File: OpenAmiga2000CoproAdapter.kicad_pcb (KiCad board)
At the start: 2 copper layers, 188.6 x 110.4 mm, 75 parts, among them CN1 A2000_COPRO_SLOT, P1 CONN_2, P10 CONN_1, P11 CONN_1, P12 CONN_1, P13 CONN_1, P14 CONN_1, P15 CONN_1, P2 CONN_2, P3 CONN_2, P4 CONN_2, P5 CONN_1, P6 CONN_1, P7 CONN_1, P8 CONN_1, P9 CONN_1, P99 OSHW_LOGO, U1 68000D, U10 Spare, U11 74HCT00, U12 74HCT27, U13 74HCT74, U14 74F86, U15 74F74, U16 74HCT04, U17 74HCT112, U18 74F157, U19 74F157, U2 AS6C4008-55PCN, U3 AS6C4008-55PCN, U4 AS6C4008-55PCN, U5 AS6C4008-55PCN, U6 74HCT00, U7 74HCT32, U8 74HCT32, U9 74LS05

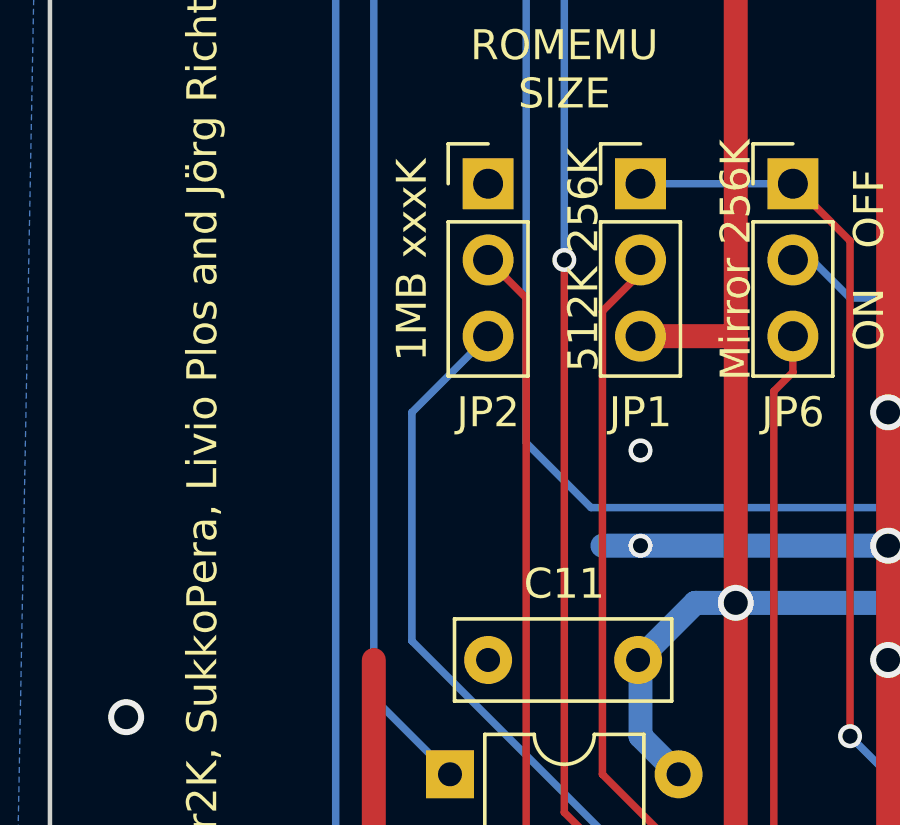
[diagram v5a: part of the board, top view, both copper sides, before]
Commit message: turn jumper around so it matches silk screen
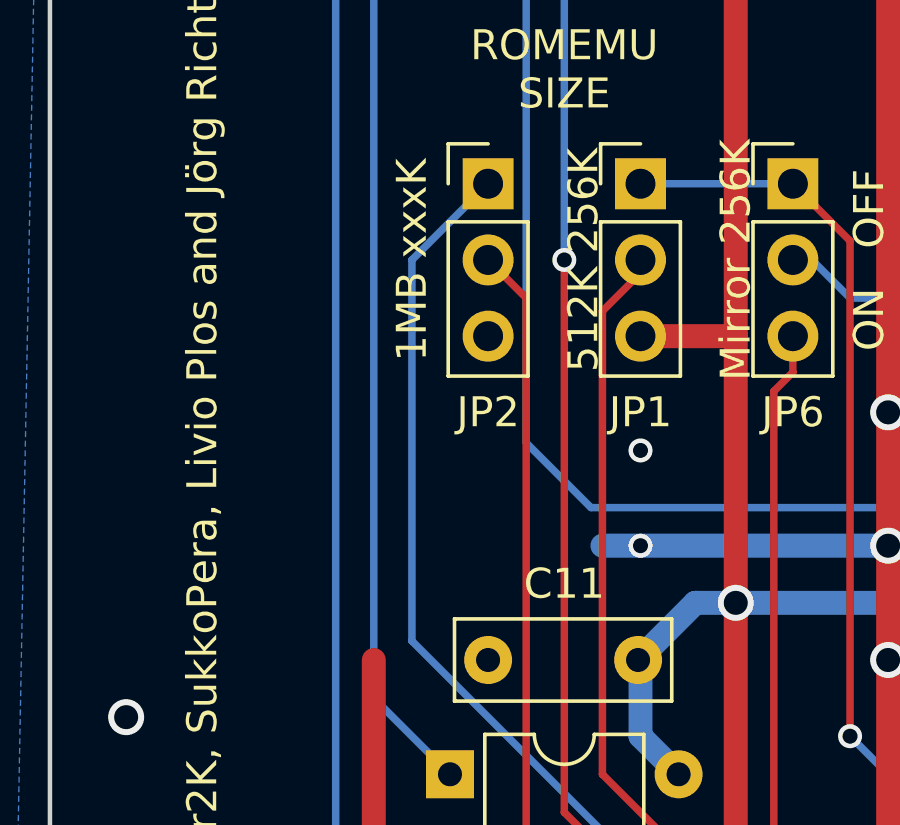
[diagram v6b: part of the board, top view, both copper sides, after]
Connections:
- JP2 pad 1: GND -> Net-(JP2-Pad1)
- JP2 pad 3: Net-(JP2-Pad3) -> GND
- JP8 pad 2: Net-(JP2-Pad3) -> Net-(JP2-Pad1)
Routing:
- net Net-(JP2-Pad1): track 0.00 -> 40.7 mm
- net Net-(JP2-Pad3): track 35.6 -> 0.00 mm
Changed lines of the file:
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@@
   (net 125 /Memory/SROMON)
   (net 126 /Memory/~OE)
-  (net 127 "Net-(JP2-Pad3)")
-  (net 128 "Net-(JP7-Pad2)")
-  (net 129 5VR)
-  (net 130 /Memory/~CRAM)
-  (net 131 "Net-(BAT1-PadPos)")
+  (net 127 "Net-(JP7-Pad2)")
+  (net 128 5VR)
+  (net 129 /Memory/~CRAM)
+  (net 130 "Net-(BAT1-PadPos)")
+  (net 131 "Net-(JP2-Pad1)")
   (net_class Default "This is the default net class."
     (clearance 0.2)
@@
     (add_net "Net-(JP1-Pad2)")
     (add_net "Net-(JP10-Pad1)")
+    (add_net "Net-(JP2-Pad1)")
     (add_net "Net-(JP2-Pad2)")
-    (add_net "Net-(JP2-Pad3)")
     (add_net "Net-(JP3-Pad1)")
     (add_net "Net-(JP5-Pad1)")
@@
     )
     (pad Pos thru_hole circle (at 20 0) (size 2.5 2.5) (drill 1.5) (layers *.Cu *.Mask)
-      (net 131 "Net-(BAT1-PadPos)"))
+      (net 130 "Net-(BAT1-PadPos)"))
     (pad Neg thru_hole rect (at 0 0) (size 2.17 2.17) (drill 1.17) (layers *.Cu *.Mask)
       (net 1 GND))
@@
     )
     (pad 2 thru_hole oval (at 12.7 0) (size 2.4 2.4) (drill 1.2) (layers *.Cu *.Mask)
-      (net 129 5VR))
+      (net 128 5VR))
     (pad 1 thru_hole circle (at 0 0) (size 2.4 2.4) (drill 1.2) (layers *.Cu *.Mask)
       (net 2 +5V))
@@
     )
     (pad 3 thru_hole oval (at 0 5.08) (size 1.7 1.7) (drill 1) (layers *.Cu *.Mask)
-      (net 129 5VR))
+      (net 128 5VR))
     (pad 2 thru_hole oval (at 0 2.54) (size 1.7 1.7) (drill 1) (layers *.Cu *.Mask)
-      (net 128 "Net-(JP7-Pad2)"))
+      (net 127 "Net-(JP7-Pad2)"))
     (pad 1 thru_hole rect (at 0 0) (size 1.7 1.7) (drill 1) (layers *.Cu *.Mask)
       (net 1 GND))
@@
       (net 118 "Net-(JP8-Pad3)"))
     (pad 2 thru_hole oval (at 0 2.54) (size 1.7 1.7) (drill 1) (layers *.Cu *.Mask)
-      (net 127 "Net-(JP2-Pad3)"))
+      (net 131 "Net-(JP2-Pad1)"))
     (pad 1 thru_hole rect (at 0 0) (size 1.7 1.7) (drill 1) (layers *.Cu *.Mask)
       (net 12 /a20))
@@
       (net 116 /Memory/ROMR~W))
     (pad 1 thru_hole rect (at 0 0) (size 1.7 1.7) (drill 1) (layers *.Cu *.Mask)
-      (net 129 5VR))
+      (net 128 5VR))
     (model ${KISYS3DMOD}/Connector_PinHeader_2.54mm.3dshapes/PinHeader_1x03_P2.54mm_Vertical.wrl
       (at (xyz 0 0 0))
@@
       (net 9 /a18))
     (pad 6 thru_hole oval (at 0 12.7) (size 1.6 1.6) (drill 0.8) (layers *.Cu *.Mask)
-      (net 130 /Memory/~CRAM))
+      (net 129 /Memory/~CRAM))
     (pad 12 thru_hole oval (at 7.62 5.08) (size 1.6 1.6) (drill 0.8) (layers *.Cu *.Mask)
       (net 121 /Memory/~a21))
@@
       (net 120 /Memory/~RAM2))
     (pad 9 thru_hole oval (at 7.62 12.7) (size 1.6 1.6) (drill 0.8) (layers *.Cu *.Mask)
-      (net 130 /Memory/~CRAM))
+      (net 129 /Memory/~CRAM))
     (pad 2 thru_hole oval (at 0 2.54) (size 1.6 1.6) (drill 0.8) (layers *.Cu *.Mask)
-      (net 130 /Memory/~CRAM))
+      (net 129 /Memory/~CRAM))
     (pad 8 thru_hole oval (at 7.62 15.24) (size 1.6 1.6) (drill 0.8) (layers *.Cu *.Mask)
       (net 38 "Net-(JP5-Pad1)"))
@@
     (pad 6 thru_hole oval (at 0 12.7) (size 1.6 1.6) (drill 0.8) (layers *.Cu *.Mask))
     (pad 12 thru_hole oval (at 7.62 5.08) (size 1.6 1.6) (drill 0.8) (layers *.Cu *.Mask)
-      (net 128 "Net-(JP7-Pad2)"))
+      (net 127 "Net-(JP7-Pad2)"))
     (pad 5 thru_hole oval (at 0 10.16) (size 1.6 1.6) (drill 0.8) (layers *.Cu *.Mask)
       (net 53 "Net-(U13-Pad5)"))
@@
     )
     (pad 3 thru_hole oval (at 0 5.08) (size 1.7 1.7) (drill 1) (layers *.Cu *.Mask)
-      (net 127 "Net-(JP2-Pad3)"))
+      (net 1 GND))
     (pad 2 thru_hole oval (at 0 2.54) (size 1.7 1.7) (drill 1) (layers *.Cu *.Mask)
       (net 37 "Net-(JP2-Pad2)"))
     (pad 1 thru_hole rect (at 0 0) (size 1.7 1.7) (drill 1) (layers *.Cu *.Mask)
-      (net 1 GND))
+      (net 131 "Net-(JP2-Pad1)"))
     (model ${KISYS3DMOD}/Connector_PinHeader_2.54mm.3dshapes/PinHeader_1x03_P2.54mm_Vertical.wrl
       (at (xyz 0 0 0))
@@
     )
     (pad 2 thru_hole oval (at 7.62 0 180) (size 1.8 1.8) (drill 0.9) (layers *.Cu *.Mask)
-      (net 131 "Net-(BAT1-PadPos)"))
+      (net 130 "Net-(BAT1-PadPos)"))
     (pad 1 thru_hole rect (at 0 0 180) (size 1.8 1.8) (drill 0.9) (layers *.Cu *.Mask)
       (net 29 /Memory/VSRAM))
@@
   (segment (start 81.8515 104.14) (end 81.8515 124.656998) (width 0.25) (layer F.Cu) (net 126))
   (segment (start 79.9465 102.235) (end 81.8515 104.14) (width 0.25) (layer F.Cu) (net 126))
-  (segment (start 53.2765 87.63) (end 53.2765 80.01) (width 0.25) (layer B.Cu) (net 127))
-  (segment (start 60.2615 94.615) (end 53.2765 87.63) (width 0.25) (layer B.Cu) (net 127))
-  (segment (start 60.2615 100.33) (end 60.2615 94.615) (width 0.25) (layer B.Cu) (net 127))
-  (segment (start 60.8965 100.965) (end 60.2615 100.33) (width 0.25) (layer B.Cu) (net 127))
-  (segment (start 63.4365 100.965) (end 60.8965 100.965) (width 0.25) (layer B.Cu) (net 127))
-  (segment (start 53.2765 80.01) (end 55.8165 77.47) (width 0.25) (layer B.Cu) (net 127))
-  (segment (start 67.2465 104.775) (end 63.4365 100.965) (width 0.25) (layer B.Cu) (net 127))
-  (segment (start 225.9965 44.45) (end 224.0915 42.545) (width 0.25) (layer F.Cu) (net 128))
-  (segment (start 225.9965 55.245) (end 225.9965 44.45) (width 0.25) (layer F.Cu) (net 128))
-  (segment (start 222.8215 56.515) (end 224.7265 56.515) (width 0.25) (layer F.Cu) (net 128))
-  (segment (start 224.7265 56.515) (end 225.9965 55.245) (width 0.25) (layer F.Cu) (net 128))
-  (segment (start 219.0115 52.705) (end 222.8215 56.515) (width 0.25) (layer F.Cu) (net 128))
-  (segment (start 210.7565 52.705) (end 219.0115 52.705) (width 0.25) (layer F.Cu) (net 128))
-  (segment (start 216.4715 38.735) (end 217.7415 40.005) (width 0.25) (layer F.Cu) (net 129))
-  (segment (start 208.8515 38.735) (end 216.4715 38.735) (width 0.25) (layer F.Cu) (net 129))
-  (segment (start 219.0115 40.005) (end 224.0915 45.085) (width 0.25) (layer F.Cu) (net 129))
-  (segment (start 217.7415 40.005) (end 219.0115 40.005) (width 0.25) (layer F.Cu) (net 129))
-  (segment (start 62.1665 132.08) (end 54.5465 132.08) (width 0.25) (layer B.Cu) (net 130))
-  (segment (start 54.5465 132.08) (end 52.6415 130.175) (width 0.25) (layer B.Cu) (net 130))
-  (segment (start 52.6415 123.825) (end 54.5465 121.92) (width 0.25) (layer B.Cu) (net 130))
-  (segment (start 52.6415 130.175) (end 52.6415 123.825) (width 0.25) (layer B.Cu) (net 130))
-  (segment (start 80.8965 50.8) (end 77.7215 47.625) (width 0.25) (layer F.Cu) (net 131))
-  (segment (start 82.4865 50.8) (end 80.8965 50.8) (width 0.25) (layer F.Cu) (net 131))
+  (segment (start 225.9965 44.45) (end 224.0915 42.545) (width 0.25) (layer F.Cu) (net 127))
+  (segment (start 225.9965 55.245) (end 225.9965 44.45) (width 0.25) (layer F.Cu) (net 127))
+  (segment (start 222.8215 56.515) (end 224.7265 56.515) (width 0.25) (layer F.Cu) (net 127))
+  (segment (start 224.7265 56.515) (end 225.9965 55.245) (width 0.25) (layer F.Cu) (net 127))
+  (segment (start 219.0115 52.705) (end 222.8215 56.515) (width 0.25) (layer F.Cu) (net 127))
+  (segment (start 210.7565 52.705) (end 219.0115 52.705) (width 0.25) (layer F.Cu) (net 127))
+  (segment (start 216.4715 38.735) (end 217.7415 40.005) (width 0.25) (layer F.Cu) (net 128))
+  (segment (start 208.8515 38.735) (end 216.4715 38.735) (width 0.25) (layer F.Cu) (net 128))
+  (segment (start 219.0115 40.005) (end 224.0915 45.085) (width 0.25) (layer F.Cu) (net 128))
+  (segment (start 217.7415 40.005) (end 219.0115 40.005) (width 0.25) (layer F.Cu) (net 128))
+  (segment (start 62.1665 132.08) (end 54.5465 132.08) (width 0.25) (layer B.Cu) (net 129))
+  (segment (start 54.5465 132.08) (end 52.6415 130.175) (width 0.25) (layer B.Cu) (net 129))
+  (segment (start 52.6415 123.825) (end 54.5465 121.92) (width 0.25) (layer B.Cu) (net 129))
+  (segment (start 52.6415 130.175) (end 52.6415 123.825) (width 0.25) (layer B.Cu) (net 129))
+  (segment (start 80.8965 50.8) (end 77.7215 47.625) (width 0.25) (layer F.Cu) (net 130))
+  (segment (start 82.4865 50.8) (end 80.8965 50.8) (width 0.25) (layer F.Cu) (net 130))
+  (segment (start 53.2765 74.93) (end 55.8165 72.39) (width 0.25) (layer B.Cu) (net 131))
+  (segment (start 53.2765 87.63) (end 53.2765 74.93) (width 0.25) (layer B.Cu) (net 131))
+  (segment (start 60.2615 94.615) (end 53.2765 87.63) (width 0.25) (layer B.Cu) (net 131))
+  (segment (start 60.2615 100.33) (end 60.2615 94.615) (width 0.25) (layer B.Cu) (net 131))
+  (segment (start 60.8965 100.965) (end 60.2615 100.33) (width 0.25) (layer B.Cu) (net 131))
+  (segment (start 63.4365 100.965) (end 60.8965 100.965) (width 0.25) (layer B.Cu) (net 131))
+  (segment (start 67.2465 104.775) (end 63.4365 100.965) (width 0.25) (layer B.Cu) (net 131))
   (zone (net 1) (net_name GND) (layer B.Cu) (hatch edge 0.508)
     (connect_pads (clearance 0.1))
